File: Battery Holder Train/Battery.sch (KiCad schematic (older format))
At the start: 1 part

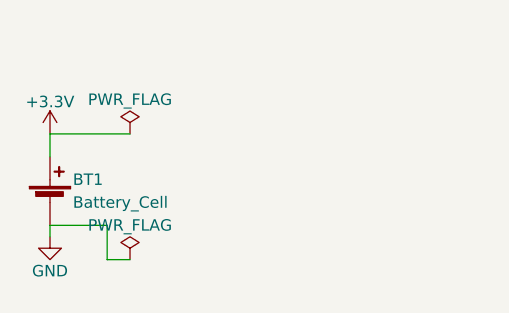
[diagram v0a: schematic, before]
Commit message: Homework extention with extra 3 battery holder types
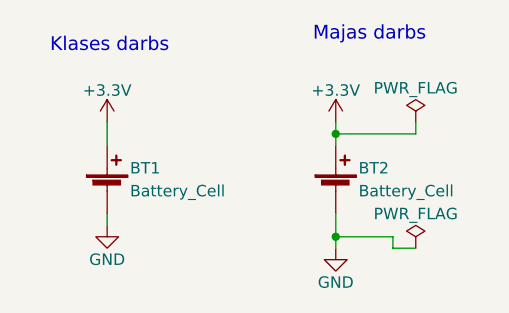
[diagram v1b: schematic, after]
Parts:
- added BT2: Battery_Cell, Battery_holders:Keystone_1066_20mm, symbol Battery_Cell
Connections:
- net +3V3: now also BT2.1 (+)
- net GND: now also BT2.2 (-)
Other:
- note added: "Klases darbs\n"
- note added: "Majas darbs"
- moved on the sheet: BT1
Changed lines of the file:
@@
 L Battery_Cell BT1
 U 1 1 5AB37907
-P 3050 3750
-F 0 "BT1" H 3150 3850 50  0000 L CNN
-F 1 "Battery_Cell" H 3150 3750 50  0000 L CNN
-F 2 "Battery_holders:S8211R" V 3050 3810 50  0001 C CNN
-F 3 "" V 3050 3810 50  0001 C CNN
-	1    3050 3750
+P 3300 3700
+F 0 "BT1" H 3400 3800 50  0000 L CNN
+F 1 "Battery_Cell" H 3400 3700 50  0000 L CNN
+F 2 "Battery_holders:S8211R" V 3300 3760 50  0001 C CNN
+F 3 "" V 3300 3760 50  0001 C CNN
+	1    3300 3700
 	1    0    0    -1
 $EndComp
@@
 L GND #PWR01
 U 1 1 5AB37926
-P 3050 3900
-F 0 "#PWR01" H 3050 3650 50  0001 C CNN
-F 1 "GND" H 3050 3750 50  0000 C CNN
-F 2 "" H 3050 3900 50  0001 C CNN
-F 3 "" H 3050 3900 50  0001 C CNN
-	1    3050 3900
+P 3300 3850
+F 0 "#PWR01" H 3300 3600 50  0001 C CNN
+F 1 "GND" H 3300 3700 50  0000 C CNN
+F 2 "" H 3300 3850 50  0001 C CNN
+F 3 "" H 3300 3850 50  0001 C CNN
+	1    3300 3850
 	1    0    0    -1
 $EndComp
@@
 L +3.3V #PWR02
 U 1 1 5AB3793C
-P 3050 3450
-F 0 "#PWR02" H 3050 3300 50  0001 C CNN
-F 1 "+3.3V" H 3050 3590 50  0000 C CNN
-F 2 "" H 3050 3450 50  0001 C CNN
-F 3 "" H 3050 3450 50  0001 C CNN
-	1    3050 3450
+P 3300 3400
+F 0 "#PWR02" H 3300 3250 50  0001 C CNN
+F 1 "+3.3V" H 3300 3540 50  0000 C CNN
+F 2 "" H 3300 3400 50  0001 C CNN
+F 3 "" H 3300 3400 50  0001 C CNN
+	1    3300 3400
 	1    0    0    -1
 $EndComp
 Wire Wire Line
-	3050 3450 3050 3550
+	3300 3400 3300 3500
 Wire Wire Line
-	3050 3850 3050 3900
+	3300 3800 3300 3850
 $Comp
-L PWR_FLAG #FLG03
-U 1 1 5AB37970
-P 3400 3450
-F 0 "#FLG03" H 3400 3525 50  0001 C CNN
-F 1 "PWR_FLAG" H 3400 3600 50  0000 C CNN
-F 2 "" H 3400 3450 50  0001 C CNN
-F 3 "" H 3400 3450 50  0001 C CNN
-	1    3400 3450
+L Battery_Cell BT2
+U 1 1 5AB95309
+P 4300 3700
+F 0 "BT2" H 4400 3800 50  0000 L CNN
+F 1 "Battery_Cell" H 4400 3700 50  0000 L CNN
+F 2 "Battery_holders:Keystone_1066_20mm" V 4300 3760 50  0001 C CNN
+F 3 "" V 4300 3760 50  0001 C CNN
+	1    4300 3700
 	1    0    0    -1
 $EndComp
 $Comp
-L PWR_FLAG #FLG04
-U 1 1 5AB37985
-P 3400 4000
-F 0 "#FLG04" H 3400 4075 50  0001 C CNN
-F 1 "PWR_FLAG" H 3400 4150 50  0000 C CNN
-F 2 "" H 3400 4000 50  0001 C CNN
-F 3 "" H 3400 4000 50  0001 C CNN
-	1    3400 4000
+L +3.3V #PWR03
+U 1 1 5AB95331
+P 4300 3400
+F 0 "#PWR03" H 4300 3250 50  0001 C CNN
+F 1 "+3.3V" H 4300 3540 50  0000 C CNN
+F 2 "" H 4300 3400 50  0001 C CNN
+F 3 "" H 4300 3400 50  0001 C CNN
+	1    4300 3400
+	1    0    0    -1
+$EndComp
+$Comp
+L GND #PWR04
+U 1 1 5AB95342
+P 4300 3950
+F 0 "#PWR04" H 4300 3700 50  0001 C CNN
+F 1 "GND" H 4300 3800 50  0000 C CNN
+F 2 "" H 4300 3950 50  0001 C CNN
+F 3 "" H 4300 3950 50  0001 C CNN
+	1    4300 3950
+	1    0    0    -1
+$EndComp
+$Comp
+L PWR_FLAG #FLG05
+U 1 1 5AB95353
+P 4650 3950
+F 0 "#FLG05" H 4650 4025 50  0001 C CNN
+F 1 "PWR_FLAG" H 4650 4100 50  0000 C CNN
+F 2 "" H 4650 3950 50  0001 C CNN
+F 3 "" H 4650 3950 50  0001 C CNN
+	1    4650 3950
+	1    0    0    -1
+$EndComp
+$Comp
+L PWR_FLAG #FLG06
+U 1 1 5AB95364
+P 4650 3400
+F 0 "#FLG06" H 4650 3475 50  0001 C CNN
+F 1 "PWR_FLAG" H 4650 3550 50  0000 C CNN
+F 2 "" H 4650 3400 50  0001 C CNN
+F 3 "" H 4650 3400 50  0001 C CNN
+	1    4650 3400
 	1    0    0    -1
 $EndComp
 Wire Wire Line
-	3400 3450 3050 3450
+	4300 3400 4300 3500
 Wire Wire Line
-	3050 3850 3300 3850
+	4300 3800 4300 3950
 Wire Wire Line
-	3300 3850 3300 4000
+	4300 3900 4550 3900
 Wire Wire Line
-	3300 4000 3400 4000
+	4550 3900 4550 3950
+Wire Wire Line
+	4550 3950 4650 3950
+Connection ~ 4300 3900
+Wire Wire Line
+	4300 3450 4650 3450
+Wire Wire Line
+	4650 3450 4650 3400
+Connection ~ 4300 3450
+Text Notes 3050 3100 0    60   ~ 0
+Klases darbs\n
+Text Notes 4200 3050 0    60   ~ 0
+Majas darbs
 $EndSCHEMATC
